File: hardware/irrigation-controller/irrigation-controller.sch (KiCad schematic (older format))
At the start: 83 parts, among them J1 RS485, J10 I2C, J11 IO, J12 RELAY_2, J15 FLOW_1, J2 I2C, J3 ICSP, J4 UART, J5 RF Module, J6 PWR 24V, J7 RELAY_1, J8 RELAY_3, J9 RELAY_4, K1 RELAY_3, K2 RELAY_4, Q1 MMBT3904, Q2 MMBT3904, Q3 2N7002, Q4 2N7002, Q5 2N7002, Q6 2N7002, SW1 RESET, SW2 BUTTON, U1 AQY280EH, U2 ATmega328P-AU, U3 AQY280EH, U4 TPS54331DR, U5 TPS54331DR, U6 MAX485, Y1 8MHz

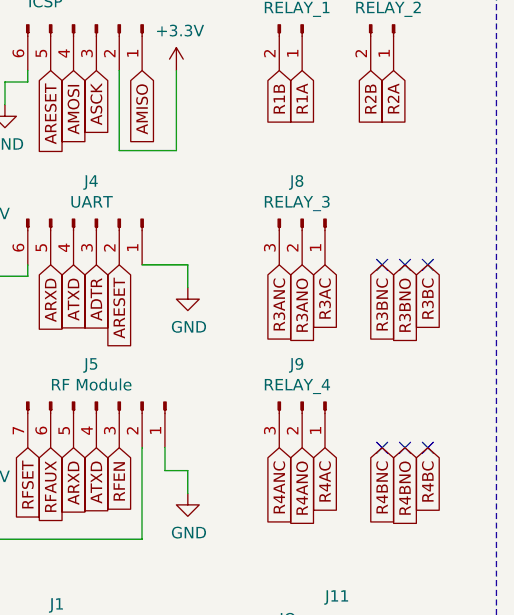
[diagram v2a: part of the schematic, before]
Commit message: Route all controller board nets
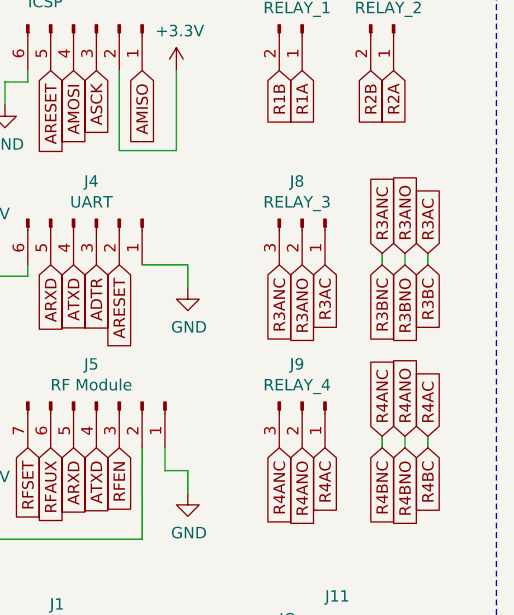
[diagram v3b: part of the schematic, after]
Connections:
- net R3BC is gone; now on net R3AC: K1.6
- net R3BNC is gone; now on net R3ANC: K1.7
- net R3BNO is gone; now on net R3ANO: K1.5
- net R4BC is gone; now on net R4AC: K2.6
- net R4BNC is gone; now on net R4ANC: K2.7
- net R4BNO is gone; now on net R4ANO: K2.5
- no-connect marks 10 -> 4
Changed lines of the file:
@@
 Wire Wire Line
 	9100 1150 9100 1100
-NoConn ~ 10650 1950
-NoConn ~ 10750 1950
-NoConn ~ 10850 1950
-NoConn ~ 10650 2750
-NoConn ~ 10750 2750
-NoConn ~ 10850 2750
 $Comp
 L Mechanical:MountingHole_Pad H1
@@
 	9800 5650 9800 5600
 Connection ~ 9800 5600
+Text GLabel 10850 1900 1    50   Input ~ 0
+R3AC
+Text GLabel 10750 1900 1    50   Input ~ 0
+R3ANO
+Text GLabel 10650 1900 1    50   Input ~ 0
+R3ANC
+Text GLabel 10850 2700 1    50   Input ~ 0
+R4AC
+Text GLabel 10750 2700 1    50   Input ~ 0
+R4ANO
+Text GLabel 10650 2700 1    50   Input ~ 0
+R4ANC
+Wire Wire Line
+	10650 1900 10650 1950
+Wire Wire Line
+	10750 1900 10750 1950
+Wire Wire Line
+	10850 1900 10850 1950
+Wire Wire Line
+	10650 2700 10650 2750
+Wire Wire Line
+	10750 2700 10750 2750
+Wire Wire Line
+	10850 2700 10850 2750
 $EndSCHEMATC
